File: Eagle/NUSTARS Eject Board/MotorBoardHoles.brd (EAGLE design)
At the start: 44.4 x 40.3 mm, 13 parts, among them Q1 200mA/40V

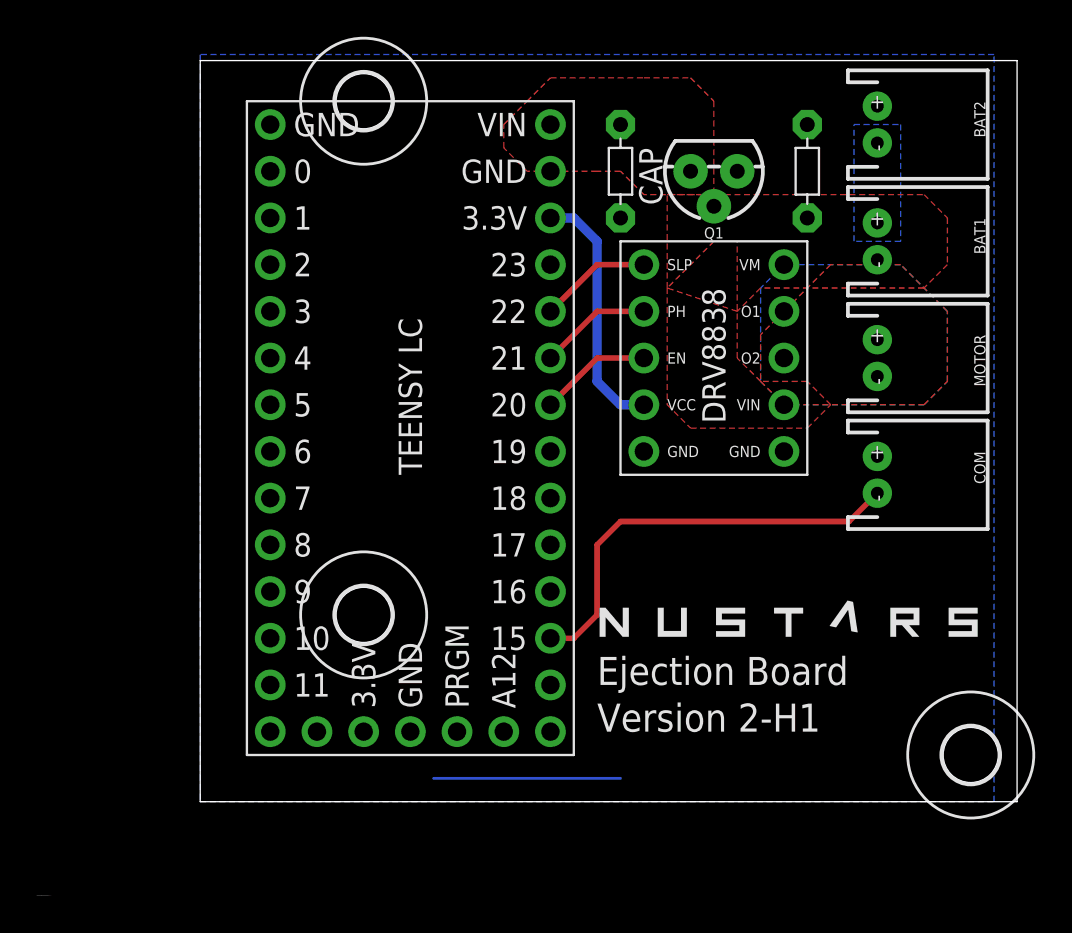
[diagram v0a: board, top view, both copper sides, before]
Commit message: Add rover
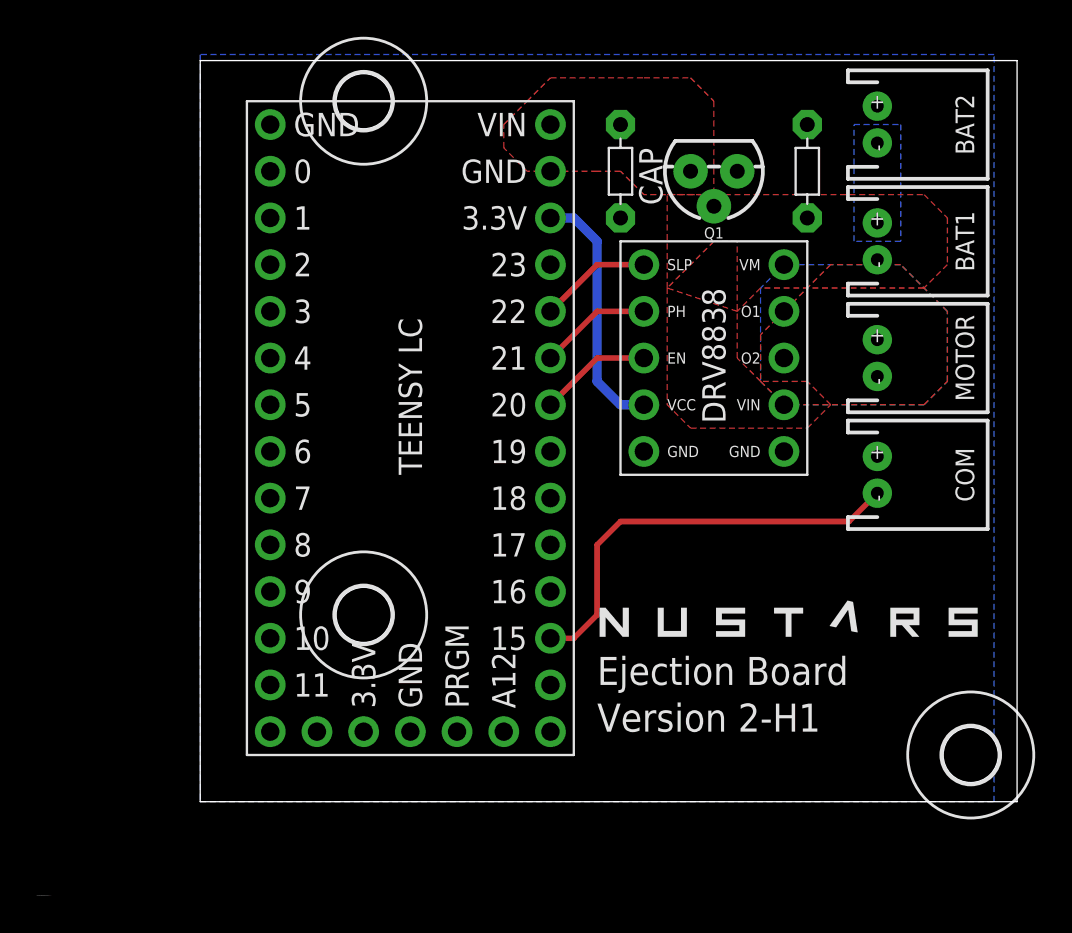
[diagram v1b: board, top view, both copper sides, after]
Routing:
- net GND: track 10.2 -> 0.00 mm
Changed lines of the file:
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@@
 <setting verticaltext="up"/>
 </settings>
-<grid distance="0.3" unitdist="mil" unit="mil" style="lines" multiple="1" display="yes" altdistance="5" altunitdist="mil" altunit="mil"/>
+<grid distance="10" unitdist="mil" unit="mil" style="lines" multiple="1" display="yes" altdistance="5" altunitdist="mil" altunit="mil"/>
 <layers>
 <layer number="1" name="Top" color="4" fill="1" visible="yes" active="yes"/>
@@
 <layer number="21" name="tPlace" color="7" fill="1" visible="yes" active="yes"/>
 <layer number="22" name="bPlace" color="7" fill="1" visible="yes" active="yes"/>
-<layer number="23" name="tOrigins" color="15" fill="1" visible="yes" active="yes"/>
+<layer number="23" name="tOrigins" color="15" fill="1" visible="no" active="yes"/>
 <layer number="24" name="bOrigins" color="15" fill="1" visible="no" active="yes"/>
-<layer number="25" name="tNames" color="7" fill="1" visible="yes" active="yes"/>
+<layer number="25" name="tNames" color="7" fill="1" visible="no" active="yes"/>
 <layer number="26" name="bNames" color="7" fill="1" visible="no" active="yes"/>
-<layer number="27" name="tValues" color="7" fill="1" visible="yes" active="yes"/>
-<layer number="28" name="bValues" color="7" fill="1" visible="yes" active="yes"/>
+<layer number="27" name="tValues" color="7" fill="1" visible="no" active="yes"/>
+<layer number="28" name="bValues" color="7" fill="1" visible="no" active="yes"/>
 <layer number="29" name="tStop" color="7" fill="3" visible="no" active="yes"/>
 <layer number="30" name="bStop" color="7" fill="6" visible="no" active="yes"/>
@@
 </class>
 </classes>
-<designrules name="default">
-<description language="de">&lt;b&gt;EAGLE Design Rules&lt;/b&gt;
-&lt;p&gt;
-Die Standard-Design-Rules sind so gewählt, dass sie für
-die meisten Anwendungen passen. Sollte ihre Platine
-besondere Anforderungen haben, treffen Sie die erforderlichen
-Einstellungen hier und speichern die Design Rules unter
-einem neuen Namen ab.</description>
+<designrules name="SparkFun">
 <description language="en">&lt;b&gt;EAGLE Design Rules&lt;/b&gt;
 &lt;p&gt;
@@
 <param name="mtCopper" value="0.035mm 0.035mm 0.035mm 0.035mm 0.035mm 0.035mm 0.035mm 0.035mm 0.035mm 0.035mm 0.035mm 0.035mm 0.035mm 0.035mm 0.035mm 0.035mm"/>
 <param name="mtIsolate" value="1.5mm 0.15mm 0.2mm 0.15mm 0.2mm 0.15mm 0.2mm 0.15mm 0.2mm 0.15mm 0.2mm 0.15mm 0.2mm 0.15mm 0.2mm"/>
-<param name="mdWireWire" value="6mil"/>
-<param name="mdWirePad" value="6mil"/>
-<param name="mdWireVia" value="6mil"/>
-<param name="mdPadPad" value="6mil"/>
-<param name="mdPadVia" value="6mil"/>
-<param name="mdViaVia" value="6mil"/>
-<param name="mdSmdPad" value="6mil"/>
-<param name="mdSmdVia" value="6mil"/>
-<param name="mdSmdSmd" value="6mil"/>
-<param name="mdViaViaSameLayer" value="6mil"/>
+<param name="mdWireWire" value="8mil"/>
+<param name="mdWirePad" value="8mil"/>
+<param name="mdWireVia" value="8mil"/>
+<param name="mdPadPad" value="8mil"/>
+<param name="mdPadVia" value="8mil"/>
+<param name="mdViaVia" value="8mil"/>
+<param name="mdSmdPad" value="8mil"/>
+<param name="mdSmdVia" value="8mil"/>
+<param name="mdSmdSmd" value="8mil"/>
+<param name="mdViaViaSameLayer" value="8mil"/>
 <param name="mnLayersViaInSmd" value="2"/>
-<param name="mdCopperDimension" value="40mil"/>
-<param name="mdDrill" value="6mil"/>
+<param name="mdCopperDimension" value="10mil"/>
+<param name="mdDrill" value="8mil"/>
 <param name="mdSmdStop" value="0mil"/>
-<param name="msWidth" value="6mil"/>
-<param name="msDrill" value="0.35mm"/>
+<param name="msWidth" value="8mil"/>
+<param name="msDrill" value="20mil"/>
 <param name="msMicroVia" value="9.99mm"/>
 <param name="msBlindViaRatio" value="0.5"/>
@@
 <param name="rvMicroViaOuter" value="0.25"/>
 <param name="rvMicroViaInner" value="0.25"/>
-<param name="rlMinPadTop" value="10mil"/>
+<param name="rlMinPadTop" value="12mil"/>
 <param name="rlMaxPadTop" value="20mil"/>
 <param name="rlMinPadInner" value="10mil"/>
 <param name="rlMaxPadInner" value="20mil"/>
-<param name="rlMinPadBottom" value="10mil"/>
+<param name="rlMinPadBottom" value="12mil"/>
 <param name="rlMaxPadBottom" value="20mil"/>
-<param name="rlMinViaOuter" value="8mil"/>
+<param name="rlMinViaOuter" value="10mil"/>
 <param name="rlMaxViaOuter" value="20mil"/>
-<param name="rlMinViaInner" value="8mil"/>
+<param name="rlMinViaInner" value="10mil"/>
 <param name="rlMaxViaInner" value="20mil"/>
 <param name="rlMinMicroViaOuter" value="4mil"/>
@@
 <param name="mlMinCreamFrame" value="0mil"/>
 <param name="mlMaxCreamFrame" value="0mil"/>
-<param name="mlViaStopLimit" value="0mil"/>
+<param name="mlViaStopLimit" value="25mil"/>
 <param name="srRoundness" value="0"/>
 <param name="srMinRoundness" value="0mil"/>
@@
 <element name="U$2" library="IchiCustoms" package="POLOLU_DRV8838" value="POLOLU_DRV8838" x="41.91" y="35.56" smashed="yes" rot="R180"/>
 <element name="BAT1" library="SparkFun-Connectors" library_urn="urn:adsk.eagle:library:513" package="JST-2-PTH" package3d_urn="urn:adsk.eagle:package:38053/1" value="" x="45.72" y="35.56" smashed="yes" rot="R270">
-<attribute name="NAME" x="50.99" y="36.83" size="0.6096" layer="21" font="vector" ratio="20" rot="R270"/>
+<attribute name="NAME" x="50.99" y="35.56" size="1.016" layer="21" font="vector" ratio="20" rot="R270" align="top-center"/>
 <attribute name="PROD_ID" value="CONN-09863" x="45.72" y="35.56" size="1.778" layer="27" rot="R270" display="off"/>
 <attribute name="SKU" value="PRT-09914" x="45.72" y="35.56" size="1.778" layer="27" rot="R270" display="off"/>
@@
 </element>
 <element name="BAT2" library="SparkFun-Connectors" library_urn="urn:adsk.eagle:library:513" package="JST-2-PTH" package3d_urn="urn:adsk.eagle:package:38053/1" value="" x="45.72" y="41.91" smashed="yes" rot="R270">
-<attribute name="NAME" x="50.99" y="43.18" size="0.6096" layer="21" font="vector" ratio="20" rot="R270"/>
+<attribute name="NAME" x="50.99" y="41.91" size="1.016" layer="21" font="vector" ratio="20" rot="R270" align="top-center"/>
 <attribute name="PROD_ID" value="CONN-09863" x="45.72" y="41.91" size="1.778" layer="27" rot="R270" display="off"/>
 <attribute name="SKU" value="PRT-09914" x="45.72" y="41.91" size="1.778" layer="27" rot="R270" display="off"/>
@@
 </element>
 <element name="COM" library="SparkFun-Connectors" library_urn="urn:adsk.eagle:library:513" package="JST-2-PTH" package3d_urn="urn:adsk.eagle:package:38053/1" value="" x="45.72" y="22.86" smashed="yes" rot="R270">
-<attribute name="NAME" x="50.99" y="24.13" size="0.6096" layer="21" font="vector" ratio="20" rot="R270"/>
+<attribute name="NAME" x="50.99" y="22.86" size="1.016" layer="21" font="vector" ratio="20" rot="R270" align="top-center"/>
 <attribute name="PROD_ID" value="CONN-09863" x="45.72" y="22.86" size="1.778" layer="27" rot="R270" display="off"/>
 <attribute name="SKU" value="PRT-09914" x="45.72" y="22.86" size="1.778" layer="27" rot="R270" display="off"/>
@@
 </element>
 <element name="MOTOR" library="SparkFun-Connectors" library_urn="urn:adsk.eagle:library:513" package="JST-2-PTH" package3d_urn="urn:adsk.eagle:package:38053/1" value="" x="45.72" y="29.21" smashed="yes" rot="R270">
-<attribute name="NAME" x="50.99" y="30.48" size="0.6096" layer="21" font="vector" ratio="20" rot="R270"/>
+<attribute name="NAME" x="50.99" y="29.21" size="1.016" layer="21" font="vector" ratio="20" rot="R270" align="top-center"/>
 <attribute name="PROD_ID" value="CONN-09863" x="45.72" y="29.21" size="1.778" layer="27" rot="R270" display="off"/>
 <attribute name="SKU" value="PRT-09914" x="45.72" y="29.21" size="1.778" layer="27" rot="R270" display="off"/>
@@
 <contactref element="U$2" pad="M_GND"/>
 <contactref element="U$2" pad="GND2"/>
-<wire x1="31.75" y1="6.35" x2="21.59" y2="6.35" width="0.1524" layer="16"/>
 <polygon width="0.1524" layer="16" isolate="0.3048" rank="6">
 <vertex x="8.89" y="45.72"/>
@@
 </signal>
 </signals>
+<errors>
+</errors>
 </board>
 </drawing>
